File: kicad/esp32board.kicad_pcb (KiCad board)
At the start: 2 copper layers, 28.7 x 65.5 mm, 32 parts, among them P1 ADC, P2 ADC_TOUCH, U0 SERIAL1, U1 SERIAL2

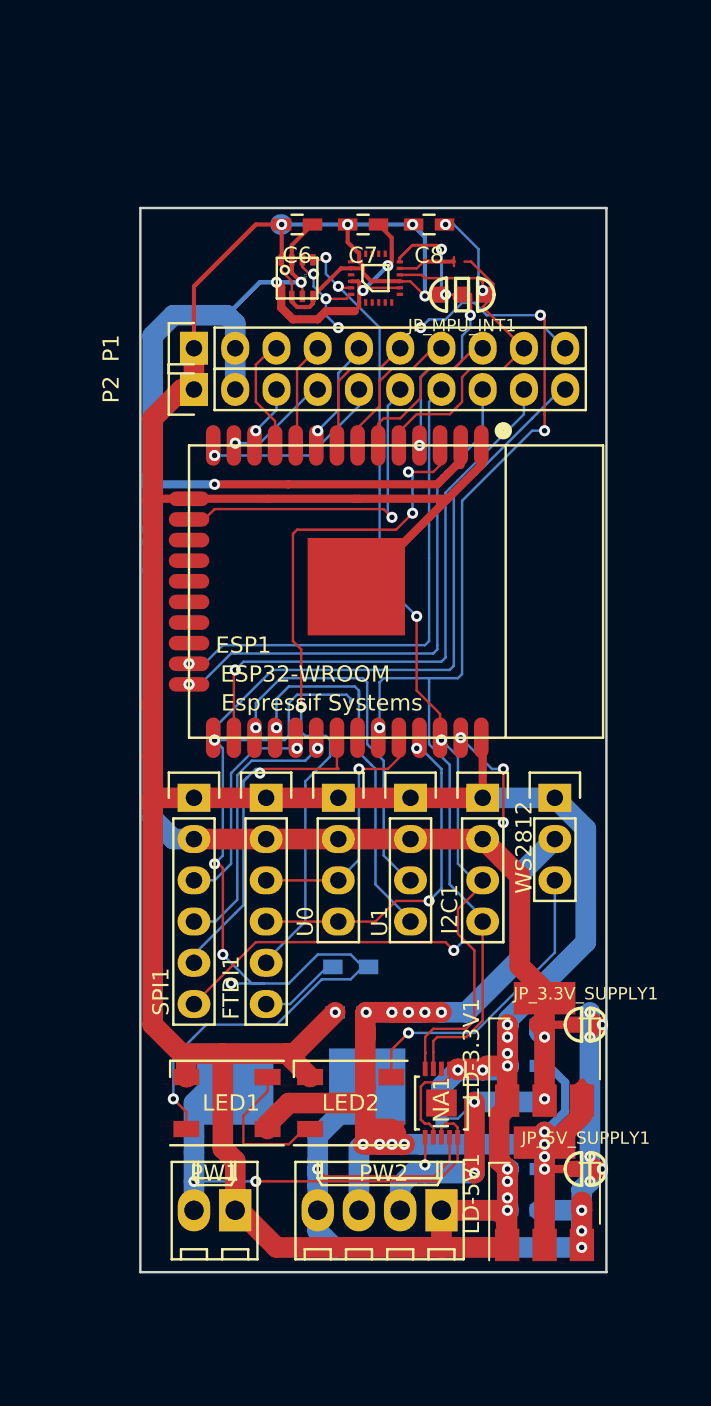
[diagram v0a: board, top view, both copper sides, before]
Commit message: Added I2S amplifier (Incomplete)
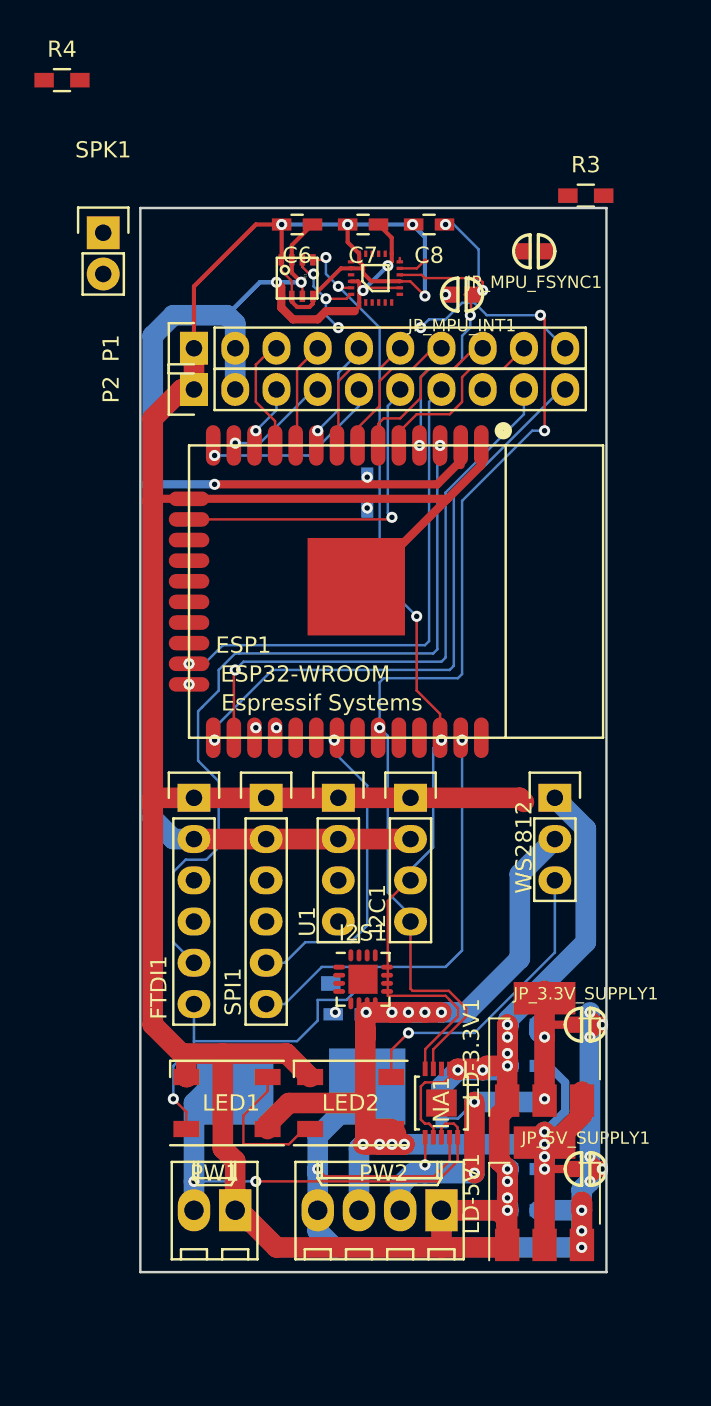
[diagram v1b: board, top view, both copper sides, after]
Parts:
- removed U0: SERIAL1, Pin_Headers:Pin_Header_Straight_1x04
- added C10: .1uF, Capacitors_SMD:C_0603_HandSoldering, B.Cu at (142.7, 124.7)
- added I2S1: MAX98357A, Housings_DFN_QFN:QFN-16-1EP_3x3mm_Pitch0.5mm, F.Cu at (142.5, 154.7)
- added JP_MPU_FSYNC1: JP_NO, jumper:SOLDER-JUMPER_1-WAY, F.Cu at (153.0, 109.9)
- added R3: 100K, Resistors_SMD:R_0603_HandSoldering, F.Cu at (156.2, 106.4)
- added R4: 100K, Resistors_SMD:R_0603_HandSoldering, F.Cu at (124.0, 99.3)
- added SPK1: CONN_SPK, Pin_Headers:Pin_Header_Straight_1x02, F.Cu at (126.5, 108.7)
- JP_MPU_INT1: footprint jumper:SOLDER-JUMPER_2-WAY -> jumper:SOLDER-JUMPER_1-WAY
- moved I2C1 4.45 mm to (145.4, 143.5)
- moved FTDI1 4.44 mm to (132.1, 143.5)
- moved SPI1 4.44 mm to (136.5, 143.5)
- moved U1 4.44 mm to (141.0, 143.5)
- moved R2 1.02 mm to (141.6, 154.9), turned to 180 degrees
- moved C9 0.18 mm to (141.6, 156.8)
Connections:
- MPU1 pad 11: (no net) -> Net-(JP_MPU_FSYNC1-Pad1)
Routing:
- net TOUCH_7: track 94.1 -> 38.6 mm, vias 5 -> 1
- net TOUCH_5: track 33.3 -> 0.00 mm
- net U2_TX: track 24.0 -> 0.68 mm
- net U2_RX: track 23.3 -> 0.65 mm
- net U0_TX: track 21.8 -> 0.99 mm, vias 2 -> 0
- net SPI_SCK: track 17.7 -> 0.57 mm, vias 1 -> 0
- net U0_RX: track 17.6 -> 1.24 mm, vias 1 -> 0
- net FTDI_DTR: track 5.77 -> 21.4 mm, vias 0 -> 1
- net 3.3V: track 158.1 -> 144.2 mm, vias 10 -> 11
- net SPI_SS: track 13.9 -> 0.57 mm, vias 1 -> 0
- net Net-(JP_MPU_INT1-Pad1): track 12.1 -> 0.54 mm, vias 2 -> 1
- net GND: track 262.4 -> 251.9 mm, vias 15 -> 16
- net SPI_MOSI: track 35.6 -> 27.3 mm, vias 4 -> 1
- net ADC_1: track 20.0 -> 12.3 mm
- net FTDI_RTS: track 45.3 -> 51.4 mm, vias 3 -> 1
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
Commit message: Finished board layout
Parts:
- removed FTDI1: CONN_FTDI, Pin_Headers:Pin_Header_Straight_1x06
- removed JP_MPU_FSYNC1, JP_MPU_INT1: JP_NO, jumper:SOLDER-JUMPER_1-WAY
- removed LED1, LED2: WS2812B_LED, LEDs:LED_WS2812B-PLCC4
- removed R2: 100K, Resistors_SMD:R_0603_HandSoldering
- added C12: .1uF, Capacitors_SMD:C_0603_HandSoldering, B.Cu at (145.4, 164.5)
- added C13: .1uF, Capacitors_SMD:C_0603_HandSoldering, B.Cu at (145.4, 162.6)
- added FSYNC1: JP_NO, jumper:SOLDER-JUMPER_1-WAY, F.Cu at (146.1, 111.8)
- added INT1: JP_NO, jumper:SOLDER-JUMPER_1-WAY, F.Cu at (148.6, 111.8)
- added P3: USB_OTG, Connectors_USB:USB_Micro-B_Molex_47346-0001, F.Cu at (151.1, 160.0)
- added PROG1: PROG, Pin_Headers:Pin_Header_Straight_1x06, F.Cu at (130.8, 146.1)
- added R5: 1K, Resistors_SMD:R_0603_HandSoldering, B.Cu at (139.2, 160.5)
- added R6: 1K, Resistors_SMD:R_0603_HandSoldering, B.Cu at (139.2, 159.0)
- added R7: 1K, Resistors_SMD:R_0603_HandSoldering, B.Cu at (139.2, 157.5)
- added R8: 1K, Resistors_SMD:R_0603_HandSoldering, B.Cu at (139.2, 156.0)
- C6, C7, C8, R3, R4: moved to B.Cu
- C9: value .1uF -> CP2102; footprint Capacitors_SMD:C_0603_HandSoldering -> Housings_DFN_QFN:QFN-28-1EP_5x5mm_Pitch0.5mm; moved to F.Cu
- SERIAL1: renamed from U1; value SERIAL2 -> SERIAL
- moved R4 64.6 mm to (139.2, 162.1)
- moved SPK1 62.7 mm to (151.1, 166.4)
- moved JP_3.3V_SUPPLY1 24.7 mm to (132.7, 165.1), turned to 90 degrees
- moved JP_5V_SUPPLY1 24.7 mm to (132.7, 174.0), turned to 90 degrees
- moved C4 23.7 mm to (129.5, 163.8)
- moved C1 23.7 mm to (129.5, 175.3)
- moved C2 23.7 mm to (129.5, 172.7)
- moved C3 23.7 mm to (129.5, 166.4)
- moved LD-3.3V1 23.7 mm to (130.8, 165.1)
- moved LD-5V1 23.7 mm to (130.8, 174.0)
- moved PW1 17.5 mm to (151.1, 174.6)
- moved R3 15.9 mm to (141.2, 111.8), turned to 90 degrees
- moved I2S1 13.9 mm to (145.4, 168.3)
- moved C5 10.4 mm to (137.2, 164.5), turned to 180 degrees
- moved INA1 10.2 mm to (139.1, 168.3), turned to 180 degrees
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- renumbered WS2812 to WS1
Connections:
- C9 pad 1: 5V -> (no net)
- C9 pad 2: GND -> (no net)
- ESP1 pad 25: TOUCH_7 -> PROG_DTR
- ESP1 pad 3: FTDI_RTS -> PROG_RTS
- ESP1 pad 33: SDA -> SPI_MOSI
- ESP1 pad 34: U0_RX -> PROG_TX
- ESP1 pad 35: U0_TX -> PROG_RX
- ESP1 pad 37: SPI_MOSI -> SDA
- I2S1 pad 1: ADC_0 -> ADC_5
- I2S1 pad 14: ADC_1 -> ADC_3
- I2S1 pad 16: ADC_2 -> ADC_4
- I2S1 pad 17: (no net) -> GND
- P2 pad 10: TOUCH_7 -> PROG_DTR
- WS1 pad 3: WS2812_OUT -> PROG_DTR
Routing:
- net PROG_DTR: track 0.00 -> 95.9 mm, vias 0 -> 2
- net Vin: track 83.9 -> 25.7 mm, vias 10 -> 3
- net ADC_5: track 7.07 -> 62.7 mm, vias 1 -> 4
- net PROG_RTS: track 0.00 -> 54.4 mm, vias 0 -> 5
- net ADC_3: track 9.17 -> 62.9 mm, vias 0 -> 4
- net ADC_4: track 8.64 -> 62.2 mm, vias 0 -> 4
- net FTDI_RTS: track 51.4 -> 0.00 mm, vias 1 -> 0
- net 3.3V: track 144.2 -> 183.8 mm
- net TOUCH_7: track 38.6 -> 0.00 mm, vias 1 -> 0
- net PROG_TX: track 0.00 -> 35.1 mm, vias 0 -> 4
- net PROG_RX: track 0.00 -> 34.3 mm, vias 0 -> 2
- net TOUCH_5: track 0.00 -> 33.7 mm
- net U2_TX: track 0.68 -> 30.7 mm, vias 1 -> 2
- net U2_RX: track 0.65 -> 29.5 mm, vias 1 -> 2
- net FTDI_DTR: track 21.4 -> 0.00 mm, vias 1 -> 0
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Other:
- board size 28.7 x 65.5 mm -> 26.7 x 69.2 mm
- net class Default: trace_width 0.1524 -> 0.254
- net class PWR: trace_width 1.27 -> 0.508
